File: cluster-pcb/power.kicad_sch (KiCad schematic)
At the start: 11 parts, among them Q301 MOSFET-N-CH-EN_100V_260mA, Q302 MOSFET-P-CH-EN_60V_50A, T301 TERM_BLK_HDR_2POS_90DEG_0.2IN, U301 TPSM365R6V5RDNR

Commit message: First steps towards v1.1
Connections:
- net VCC: no longer C303.1, U301.11 (MODE_SYNC), U301.8 (VCC)
- new net VDD: C303.1, U301.11 (MODE_SYNC), U301.8 (VCC)
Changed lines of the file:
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@@
   (title_block
     (title "cluster-pcb")
-    (date "2024-07-26")
-    (rev "1.0")
+    (date "2024-08-19")
+    (rev "1.1")
     (company "Howard Hughes Medical Institute")
   )
@@
     (effects (font (size 1.27 1.27)) (justify right bottom))
   )
-  (label "VCC" (at 187.96 57.15 180) (fields_autoplaced)
+  (label "VDD" (at 187.96 57.15 180) (fields_autoplaced)
     (effects (font (size 1.27 1.27)) (justify right bottom))
   )
@@
     (effects (font (size 1.27 1.27)) (justify left bottom))
   )
-  (label "VCC" (at 167.64 53.34 90) (fields_autoplaced)
+  (label "VDD" (at 167.64 53.34 90) (fields_autoplaced)
     (effects (font (size 1.27 1.27)) (justify left bottom))
   )
@@
     (effects (font (size 1.27 1.27)) (justify right bottom))
   )
-  (label "VCC" (at 187.96 74.93 180) (fields_autoplaced)
+  (label "VDD" (at 187.96 74.93 180) (fields_autoplaced)
     (effects (font (size 1.27 1.27)) (justify right bottom))
   )

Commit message: Update to version 1.1
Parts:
- removed Q301: MOSFET-N-CH-EN_100V_260mA, Janelia:SOT-23, symbol Janelia:MOSFET-N-CH-EN_100V_260mA
- removed R301: 1k, Janelia:R_0402_1005Metric, symbol Janelia:R_1k_0402
- removed R302: 3.6k, Janelia:R_0402_1005Metric, symbol Janelia:R_3.6k_0402
- added C305: 47uF_10V, Janelia:C_0805_2012Metric, symbol Janelia:C_47uF_10V_0805
- added D302: LED_RED, Janelia:LED_0402-1005_KNB, symbol Janelia:LED_KNB_20mA_RED_1.95V_0402
- added Q301: Transistor_BJT_NPN, Janelia:SOT-23, symbol Janelia:Transistor_BJT_MMBT5550LT1G
- added R301: 10.0k, Janelia:R_0402_1005Metric, symbol Janelia:R_10.0k_0402
- added R302: 2.7k, Janelia:R_0402_1005Metric, symbol Janelia:R_2.7k_0402
- added R303: 2.32k, Janelia:R_0805_2012Metric, symbol Janelia:R_2.32k_1W_0805
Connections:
- net +5V: now also C305.1
- net ENABLE_VCC: now also Q301.1 (B)
- net GND: now also C305.2, D302.1 (K), R302.2
- net VBB: now also R301.1, R303.1
- net ~{ENABLE_VCC}: now also Q301.3 (C), R301.2
- new net: Q301.2 (E), R302.1
- new net LED_RED+: D302.2 (A), R303.2
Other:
- note added: "(3.3V (ENABLE_VCC HIGH) - 0.6V (DIODE DROP))/2.7k = 1mA 1mA * 10k = 10V (VBB - ~{ENABLE_VCC} LOW)"
- moved on the sheet: D301, Q302, T301

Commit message: Update schematic
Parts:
- removed Q301: Transistor_BJT_NPN, Janelia:SOT-23, symbol Janelia:Transistor_BJT_MMBT5550LT1G
- removed Q302: MOSFET-P-CH-EN_60V_50A, Janelia:TO-252-2, symbol Janelia:MOSFET-P-CH-EN_60V_50A
- removed R301: 10.0k, Janelia:R_0402_1005Metric, symbol Janelia:R_10.0k_0402
- removed R302: 2.7k, Janelia:R_0402_1005Metric, symbol Janelia:R_2.7k_0402
- renumbered R303 to R301
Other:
- note removed: "(3.3V (ENABLE_VCC HIGH) - 0.6V (DIODE DROP))/2.7k = 1mA 1mA * 10k = 10V (VBB - ~{ENABLE_VCC} LOW)"
- moved on the sheet: C301, C302, C303, C304, C305, D301, D302, R301, T301, U301

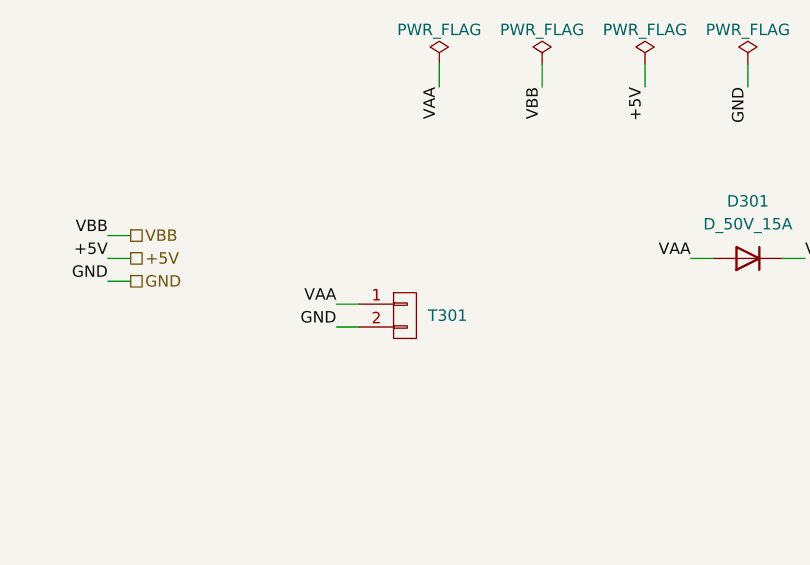
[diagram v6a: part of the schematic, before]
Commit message: Fix ERC issues
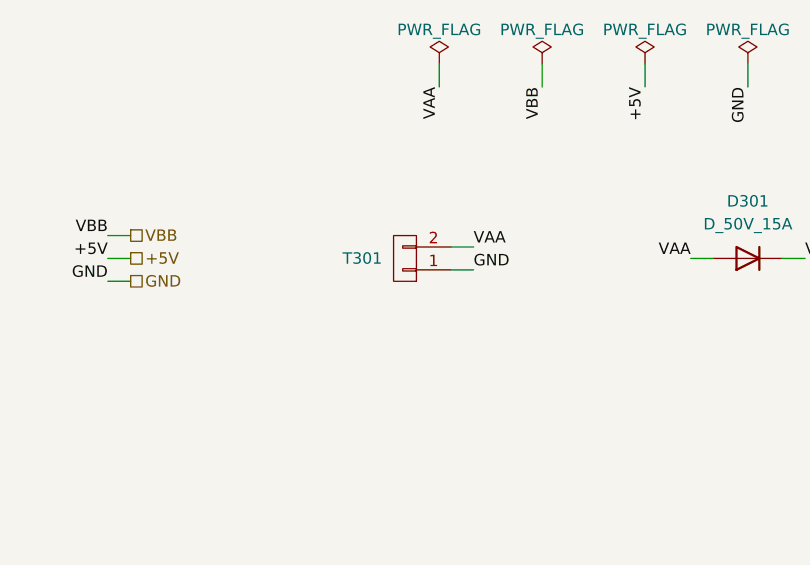
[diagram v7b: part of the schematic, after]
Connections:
- net GND: now also T301.1 (P1); no longer T301.2 (P2)
- net VAA: now also T301.2 (P2); no longer T301.1 (P1)
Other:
- moved on the sheet: T301
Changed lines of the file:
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@@
   (title_block
     (title "cluster-pcb")
-    (date "2024-09-12")
+    (date "2024-09-13")
     (rev "1.2")
     (company "Howard Hughes Medical Institute")
@@
     (stroke (width 0) (type default))
   )
-  (wire (pts (xy 119.38 73.66) (xy 116.84 73.66))
-    (stroke (width 0) (type default))
-  )
-  (wire (pts (xy 119.38 76.2) (xy 116.84 76.2))
+  (wire (pts (xy 129.54 69.85) (xy 132.08 69.85))
+    (stroke (width 0) (type default))
+  )
+  (wire (pts (xy 129.54 67.31) (xy 132.08 67.31))
     (stroke (width 0) (type default))
   )
@@
     (effects (font (size 1.27 1.27)) (justify right bottom))
   )
-  (label "GND" (at 116.84 76.2 180) (fields_autoplaced)
-    (effects (font (size 1.27 1.27)) (justify right bottom))
+  (label "GND" (at 132.08 69.85 0) (fields_autoplaced)
+    (effects (font (size 1.27 1.27)) (justify left bottom))
   )
   (label "VDD" (at 127 118.11 180) (fields_autoplaced)
@@
     (effects (font (size 1.27 1.27)) (justify right bottom))
   )
-  (label "VAA" (at 116.84 73.66 180) (fields_autoplaced)
-    (effects (font (size 1.27 1.27)) (justify right bottom))
+  (label "VAA" (at 132.08 67.31 0) (fields_autoplaced)
+    (effects (font (size 1.27 1.27)) (justify left bottom))
   )
   (label "VBB" (at 168.91 68.58 0) (fields_autoplaced)
@@
     (effects (font (size 1.27 1.27)) (justify left))
   )
-  (symbol (lib_id "Janelia:TERM_BLK_HDR_2POS_90DEG_0.2IN") (at 124.46 74.93 0) (unit 1)
+  (symbol (lib_id "Janelia:TERM_BLK_HDR_2POS_90DEG_0.2IN") (at 124.46 68.58 180) (unit 1)
     (in_bom yes) (on_board yes) (dnp no) (fields_autoplaced)
-    (property "Reference" "T301" (at 127 74.93 0)
+    (property "Reference" "T301" (at 121.92 68.58 0)
       (effects (font (size 1.27 1.27)) (justify left))
     )
-    (property "Value" "TERM_BLK_HDR_2POS_90DEG_0.2IN" (at 127 74.93 90)
-      (effects (font (size 1.27 1.27)) hide)
-    )
-    (property "Footprint" "Janelia:PHOENIX_1757242" (at 121.92 73.66 0)
-      (effects (font (size 1.524 1.524)) hide)
-    )
-    (property "Datasheet" "" (at 124.46 74.93 0)
-      (effects (font (size 1.524 1.524)) hide)
-    )
-    (property "Vendor" "Digi-Key" (at 127 68.58 0)
-      (effects (font (size 1.524 1.524)) hide)
-    )
-    (property "Vendor Part Number" "277-1106-ND" (at 129.54 66.04 0)
-      (effects (font (size 1.524 1.524)) hide)
-    )
-    (property "Synopsis" "TERM BLOCK HDR 2POS 90DEG 5.08MM" (at 132.08 63.5 0)
-      (effects (font (size 1.524 1.524)) hide)
-    )
-    (property "Manufacturer" "Phoenix Contact" (at 124.46 74.93 0)
-      (effects (font (size 1.27 1.27)) hide)
-    )
-    (property "Manufacturer Part Number" "1757242" (at 124.46 74.93 0)
-      (effects (font (size 1.27 1.27)) hide)
-    )
-    (property "Sim.Enable" "0" (at 124.46 74.93 0)
-      (effects (font (size 1.27 1.27)) hide)
-    )
-    (property "LCSC" "C90074" (at 124.46 74.93 0)
-      (effects (font (size 1.27 1.27)) hide)
-    )
-    (property "Package" "Push-Pull P=5.08mm" (at 124.46 74.93 0)
-      (effects (font (size 1.27 1.27)) hide)
-    )
+    (property "Value" "TERM_BLK_HDR_2POS_90DEG_0.2IN" (at 121.92 68.58 90)
+      (effects (font (size 1.27 1.27)) hide)
+    )
+    (property "Footprint" "Janelia:PHOENIX_1757242" (at 127 69.85 0)
+      (effects (font (size 1.524 1.524)) hide)
+    )
+    (property "Datasheet" "" (at 124.46 68.58 0)
+      (effects (font (size 1.524 1.524)) hide)
+    )
+    (property "Vendor" "Digi-Key" (at 121.92 74.93 0)
+      (effects (font (size 1.524 1.524)) hide)
+    )
+    (property "Vendor Part Number" "277-1106-ND" (at 119.38 77.47 0)
+      (effects (font (size 1.524 1.524)) hide)
+    )
+    (property "Synopsis" "TERM BLOCK HDR 2POS 90DEG 5.08MM" (at 116.84 80.01 0)
+      (effects (font (size 1.524 1.524)) hide)
+    )
+    (property "Manufacturer" "Phoenix Contact" (at 124.46 68.58 0)
+      (effects (font (size 1.27 1.27)) hide)
+    )
+    (property "Manufacturer Part Number" "1757242" (at 124.46 68.58 0)
+      (effects (font (size 1.27 1.27)) hide)
+    )
+    (property "Sim.Enable" "0" (at 124.46 68.58 0)
+      (effects (font (size 1.27 1.27)) hide)
+    )
+    (property "LCSC" "C90074" (at 124.46 68.58 0)
+      (effects (font (size 1.27 1.27)) hide)
+    )
+    (property "Package" "Push-Pull P=5.08mm" (at 124.46 68.58 0)
+      (effects (font (size 1.27 1.27)) hide)
+    )
